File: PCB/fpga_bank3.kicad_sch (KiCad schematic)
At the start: 13 parts, among them U2 XC7A50T-FGG484

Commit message: Version 1.2 routed
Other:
- title: FPGA Banks 34 & 35 -> Pi 5 - Artix XC7A50T - PCIe FPGA Hat
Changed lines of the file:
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@@
 	(paper "A4")
 	(title_block
-		(title "FPGA Banks 34 & 35")
-		(date "2024-03-24")
-		(rev "1.1")
+		(title "Pi 5 - Artix XC7A50T - PCIe FPGA Hat")
+		(date "2025-07-17")
+		(rev "1.2")
 		(company "George Smart, M1GEO")
 		(comment 1 "https://github.com/m1geo/Pi5-Artix-FPGA-Hat")

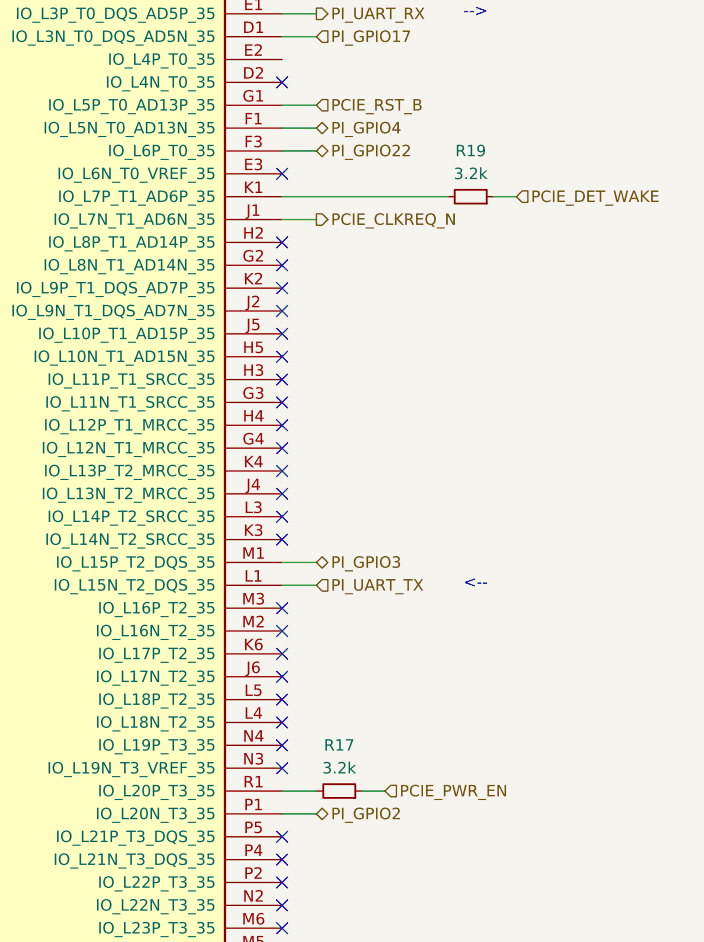
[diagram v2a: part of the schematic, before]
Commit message: Updating LEDs footprint and Resistors value
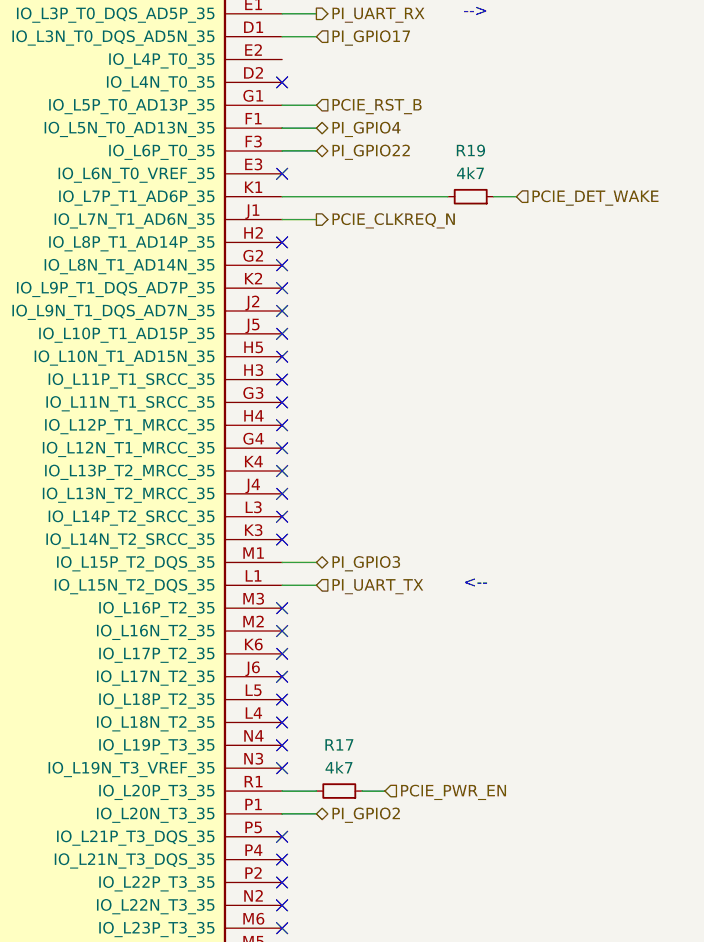
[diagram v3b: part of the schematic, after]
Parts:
- R17, R19: value 3.2k -> 4k7; LCSC C853935 -> C25900
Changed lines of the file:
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@@
 			)
 		)
-		(property "Value" "3.2k"
+		(property "Value" "4k7"
 			(at 185.42 76.2 90)
 			(effects
@@
 			)
 		)
-		(property "LCSC" "C853935"
+		(property "LCSC" "C25900"
 			(at 185.42 78.74 0)
 			(effects
@@
 			)
 		)
-		(property "Value" "3.2k"
+		(property "Value" "4k7"
 			(at 170.815 142.24 90)
 			(effects
@@
 			)
 		)
-		(property "LCSC" "C853935"
+		(property "LCSC" "C25900"
 			(at 170.815 144.78 0)
 			(effects
